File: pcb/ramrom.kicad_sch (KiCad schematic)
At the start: 18 parts, among them U11 HM628512, U12 HM628512, U13 HM628512, U14 HM628512, U15 HM628512, U16 HM628512, U17 HM628512, U18 HM628512, U21 W29C020

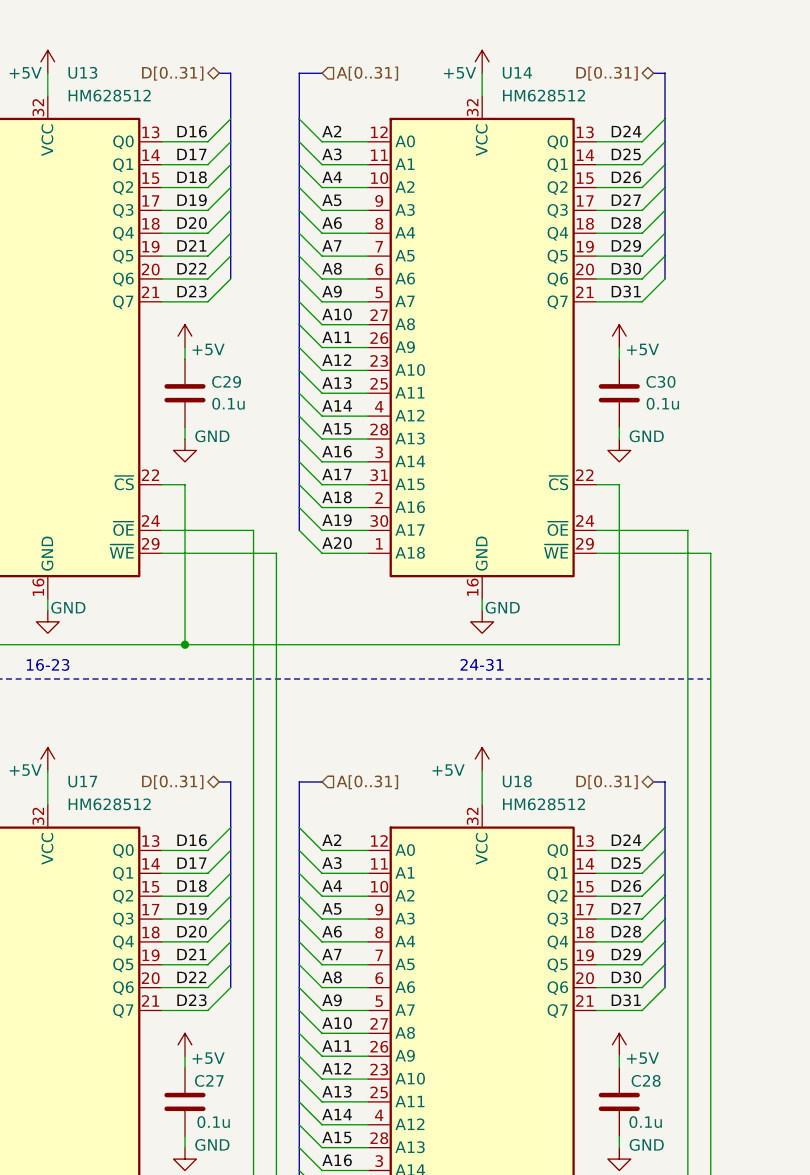
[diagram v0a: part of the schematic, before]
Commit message: reshuffled data order in upper word of ram U13 U14 U17 U18 for easier layout
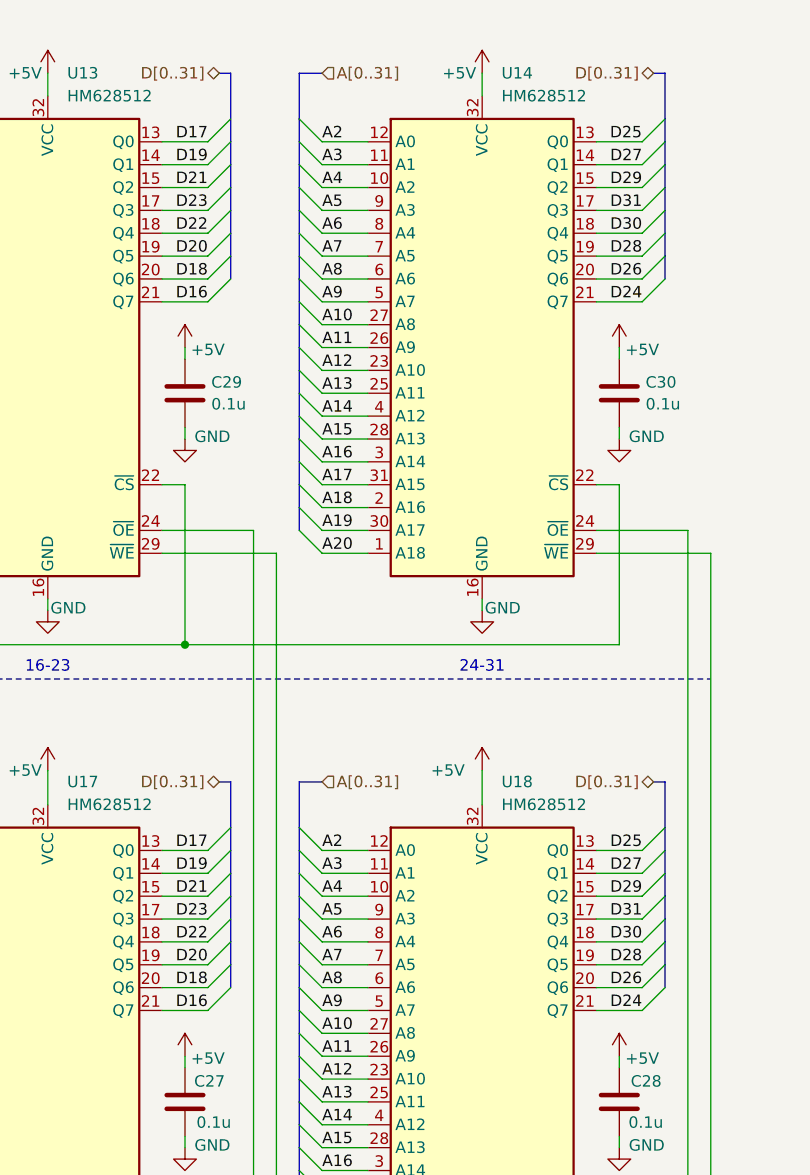
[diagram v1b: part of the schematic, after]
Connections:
- net D16: now also U13.21 (Q7), U17.21 (Q7); no longer U13.13 (Q0), U17.13 (Q0)
- net D17: now also U13.13 (Q0), U17.13 (Q0); no longer U13.14 (Q1), U17.14 (Q1)
- net D18: now also U13.20 (Q6), U17.20 (Q6); no longer U13.15 (Q2), U17.15 (Q2)
- net D19: now also U13.14 (Q1), U17.14 (Q1); no longer U13.17 (Q3), U17.17 (Q3)
- net D20: now also U13.19 (Q5), U17.19 (Q5); no longer U13.18 (Q4), U17.18 (Q4)
- net D21: now also U13.15 (Q2), U17.15 (Q2); no longer U13.19 (Q5), U17.19 (Q5)
- net D22: now also U13.18 (Q4), U17.18 (Q4); no longer U13.20 (Q6), U17.20 (Q6)
- net D23: now also U13.17 (Q3), U17.17 (Q3); no longer U13.21 (Q7), U17.21 (Q7)
- net D24: now also U14.21 (Q7), U18.21 (Q7); no longer U14.13 (Q0), U18.13 (Q0)
- net D25: now also U14.13 (Q0), U18.13 (Q0); no longer U14.14 (Q1), U18.14 (Q1)
- net D26: now also U14.20 (Q6), U18.20 (Q6); no longer U14.15 (Q2), U18.15 (Q2)
- net D27: now also U14.14 (Q1), U18.14 (Q1); no longer U14.17 (Q3), U18.17 (Q3)
- net D28: now also U14.19 (Q5), U18.19 (Q5); no longer U14.18 (Q4), U18.18 (Q4)
- net D29: now also U14.15 (Q2), U18.15 (Q2); no longer U14.19 (Q5), U18.19 (Q5)
- net D30: now also U14.18 (Q4), U18.18 (Q4); no longer U14.20 (Q6), U18.20 (Q6)
- net D31: now also U14.17 (Q3), U18.17 (Q3); no longer U14.21 (Q7), U18.21 (Q7)
